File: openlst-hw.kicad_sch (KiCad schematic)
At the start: 85 parts, among them J1 Battery, J2 CC Prog/Debug, J3 UART0, J4 SPI0, J5 Control Outputs, J6 ANT, U1 LP2981-3.3, U2 CC1110, U3 AP6502, U4 ASFL1-27.000MHZ, U5 MIC803, U6 PE4250, U8 SF2446E, U9 RFFM6404

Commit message: changed connectors, halfway through pcb
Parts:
- removed C12: 0.1u, Capacitor_SMD:C_0603_1608Metric, symbol openlst-hw:C_Small
- removed C13: 0.01u, Capacitor_SMD:C_0603_1608Metric, symbol openlst-hw:C_Small
- removed C14: 6.8n, Capacitor_SMD:C_0603_1608Metric, symbol Device:C
- removed C15, C16: 22u, Capacitor_SMD:C_1210_3225Metric, symbol Device:C
- removed C17, C18, C4: 10u, Capacitor_SMD:C_0805_2012Metric, symbol Device:C
- removed J1: Battery, TerminalBlock_Phoenix:TerminalBlock_Phoenix_MKDS-1,5-2-5.08_1x02_P5.08mm_Horizontal, symbol Connector:Screw_Terminal_01x02
- removed J2: CC Prog/Debug, Connector_PinHeader_1.27mm:PinHeader_2x05_P1.27mm_Vertical_SMD, symbol openlst-hw:Conn_02x05_Odd_Even
- removed J3: UART0, Connector_PinHeader_2.54mm:PinHeader_1x06_P2.54mm_Vertical, symbol openlst-hw:Conn_01x06
- removed J4: SPI0, Connector_PinHeader_2.54mm:PinHeader_1x06_P2.54mm_Vertical, symbol openlst-hw:Conn_01x06
- removed J5: Control Outputs, Connector_PinHeader_2.54mm:PinHeader_1x03_P2.54mm_Vertical, symbol openlst-hw:Conn_01x03
- removed L1: 10u, Inductor_SMD:L_Vishay_IFSC-1515AH_4x4x1.8mm, symbol Device:L
- removed R10, R13, R14, R9: 100, Resistor_SMD:R_0603_1608Metric, symbol openlst-hw:R
- removed R15: 6k8, Resistor_SMD:R_0603_1608Metric, symbol Device:R
- removed R19: 36k, Resistor_SMD:R_0603_1608Metric, symbol Device:R
- removed R20: 10k, Resistor_SMD:R_0603_1608Metric, symbol Device:R
- removed U1: LP2981-3.3, Package_TO_SOT_SMD:SOT-23-5, symbol Regulator_Linear:LP2985-3.3
- removed U3: AP6502, openlst:SOIC-8-1EP_3.9x4.9mm_P1.27mm_EP2.613x3.502mm, symbol Regulator_Switching:AP6502
- removed U9: RFFM6404, openlst:Qorvo_LGA_28_ThermalVias, symbol openlst-hw:RFFM6404
- added J3: Conn_02x10_Odd_Even, satfab_3rdparty:ERM8-010-YY.Y-XXX-DV-TR, symbol Connector_Generic:Conn_02x10_Odd_Even
- added U7: RFFM6406, openlst:Qorvo_LGA_28_ThermalVias, symbol openlst-hw:RFFM6406
- J6: footprint Connector_Coaxial:SMA_Samtec_SMA-J-P-X-ST-EM1_EdgeMount -> satfab_3rdparty:SAMTEC_MMCXV-J-P-HF-ST-TH1; ManufPN SMA-J-P-H-ST-EM1 -> MMCXV-J-P-HF-ST-TH1; SupplierPN SMA-J-P-H-ST-EM1 -> MMCXV-J-P-HF-ST-TH1
- L2, L3, L8: Manuf Pulse Electronics Network -> Wurth; ManufPN PE-0603FB102ST -> 74279266; SupplierPN 553-2381-1-ND -> 732-4484-1-ND
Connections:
- net +3V3: now also J3.4 (Pin_4)
- net GND: now also J3.1 (Pin_1), J3.17 (Pin_17), J3.19 (Pin_19), J3.2 (Pin_2), J3.20 (Pin_20), U7.1 (GND), U7.11 (GND), U7.12 (GND), U7.15 (GND), U7.19 (GND), U7.21 (GND), U7.22 (GND), U7.27 (GND), U7.28 (GND), U7.29 (PAD), U7.6 (GND), U7.8 (GND), U7.9 (GND)
- net LST_TX_MODE: now also U7.2 (TR)
- net PROG_DC: now also J3.16 (Pin_16)
- net PROG_DD: now also J3.18 (Pin_18)
- net RF_BYP: now also U7.4 (BYP)
- net RF_EN: now also U7.3 (EN)
- net VAA: now also J3.3 (Pin_3), J3.5 (Pin_5)
- net VAA_FILT: now also U7.17 (VCC_RX), U7.23 (VDD), U7.24 (VCC_TX1), U7.26 (VCC_TX2)
- net ~{LST_RESET}: now also J3.14 (Pin_14)
- net at C45.2: now also U7.7 (ANT)
- net at C6.1, R36.1, R37.2: now also U7.5 (VAPC)
- net at C38.2: now also U7.18 (RX)
- net at C39.2: now also U7.20 (TX)
- net at U8.2 (IN): now also U7.10 (SAW1)
- net at U8.5 (OUT): now also U7.13 (SAW2)
- net CAN_CS renamed UART1_CTS
- net CAN_MISO renamed UART1_RX
- net CAN_MOSI renamed UART1_TX
- net CAN_SCK renamed UART1_RTS
- new net UART_CTS_0: J3.12 (Pin_12)
- new net UART_RTS_0: J3.6 (Pin_6)
- new net UART_RX_0: J3.10 (Pin_10)
- new net UART_TX_0: J3.8 (Pin_8)
- no-connect marks 10 -> 9
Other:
- note removed: "4.255 V"
- note removed: "SPI Headers (3.3 V)"
- note removed: "UART Headers (3.3 V)"
- moved on the sheet: C45, H1, H2, H3, H4

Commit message: finished edits v1
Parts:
- added TP1, TP2: TestPoint, satfab:RCUCTE_0603_Test_Point, symbol Connector:TestPoint
- D1, D2, R3, R4: now not fitted
- H1, H2, H3, H4: now left out of the parts list
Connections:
- net UART_CTS_0 is gone; now on net ~{LST_RESET}: J3.12 (Pin_12)
- net UART_RTS_0 is gone; now on net UART_TX_1: J3.6 (Pin_6)
- net UART_RX_0 is gone; now on net UART_CTS_1: J3.10 (Pin_10)
- net UART_TX_0 is gone; now on net UART_RTS_1: J3.8 (Pin_8)
- net PROG_DC: now also J3.18 (Pin_18); no longer J3.16 (Pin_16)
- net PROG_DD: now also J3.16 (Pin_16); no longer J3.18 (Pin_18)
- net UART0_RX: now also TP1.1
- net UART0_TX: now also TP2.1
- net ~{LST_RESET}: no longer J3.14 (Pin_14)
- net AN1: no longer names the net of U2.6 (P0_1)
- net UART1_CTS renamed UART_CTS_1
- net UART1_RTS renamed UART_RTS_1
- net UART1_RX renamed UART_RX_1
- net UART_RX_1: now also J3.14 (Pin_14)
- net UART1_TX renamed UART_TX_1
- no-connect marks 9 -> 16

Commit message: finished edits v2
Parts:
- H1, H2, H3, H4: footprint MountingHole:MountingHole_3.2mm_M3 -> MountingHole:MountingHole_3.2mm_M3_Pad_Via; symbol Mechanical:MountingHole -> Mechanical:MountingHole_Pad; now in the parts list
- L2: footprint Inductor_SMD:L_0603_1608Metric -> Inductor_SMD:L_1206_3216Metric; Manuf Wurth -> Laird; ManufPN 74279266 -> MI1206L501R-10; SupplierPN 732-4484-1-ND -> 240-2407-2-ND
- TP1, TP2: Manuf (none) -> KOA; ManufPN (none) -> RCUCTE; Supplier (none) -> Digikey; SupplierPN (none) -> 2019-RCUCTETR-ND
- U7: Manuf (none) -> Qorvo; ManufPN (none) -> RFFM6406SR; Supplier (none) -> Mouser; SupplierPN (none) -> 772-RFFM6406SR
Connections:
- net GND: now also H1.1, H2.1, H3.1, H4.1
- net PROG_DC: now also J3.6 (Pin_6); no longer J3.18 (Pin_18)
- net PROG_DD: now also J3.8 (Pin_8); no longer J3.16 (Pin_16)
- net UART_CTS_1: now also J3.14 (Pin_14); no longer J3.10 (Pin_10)
- net UART_RTS_1: now also J3.16 (Pin_16); no longer J3.8 (Pin_8)
- net UART_RX_1: now also J3.10 (Pin_10); no longer J3.14 (Pin_14)
- net UART_TX_1: now also J3.18 (Pin_18); no longer J3.6 (Pin_6)
- no-connect marks 16 -> 15
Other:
- moved on the sheet: C1, C10, C11, C19, C2, C21, C22, C23, C24, C25, C26, C27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

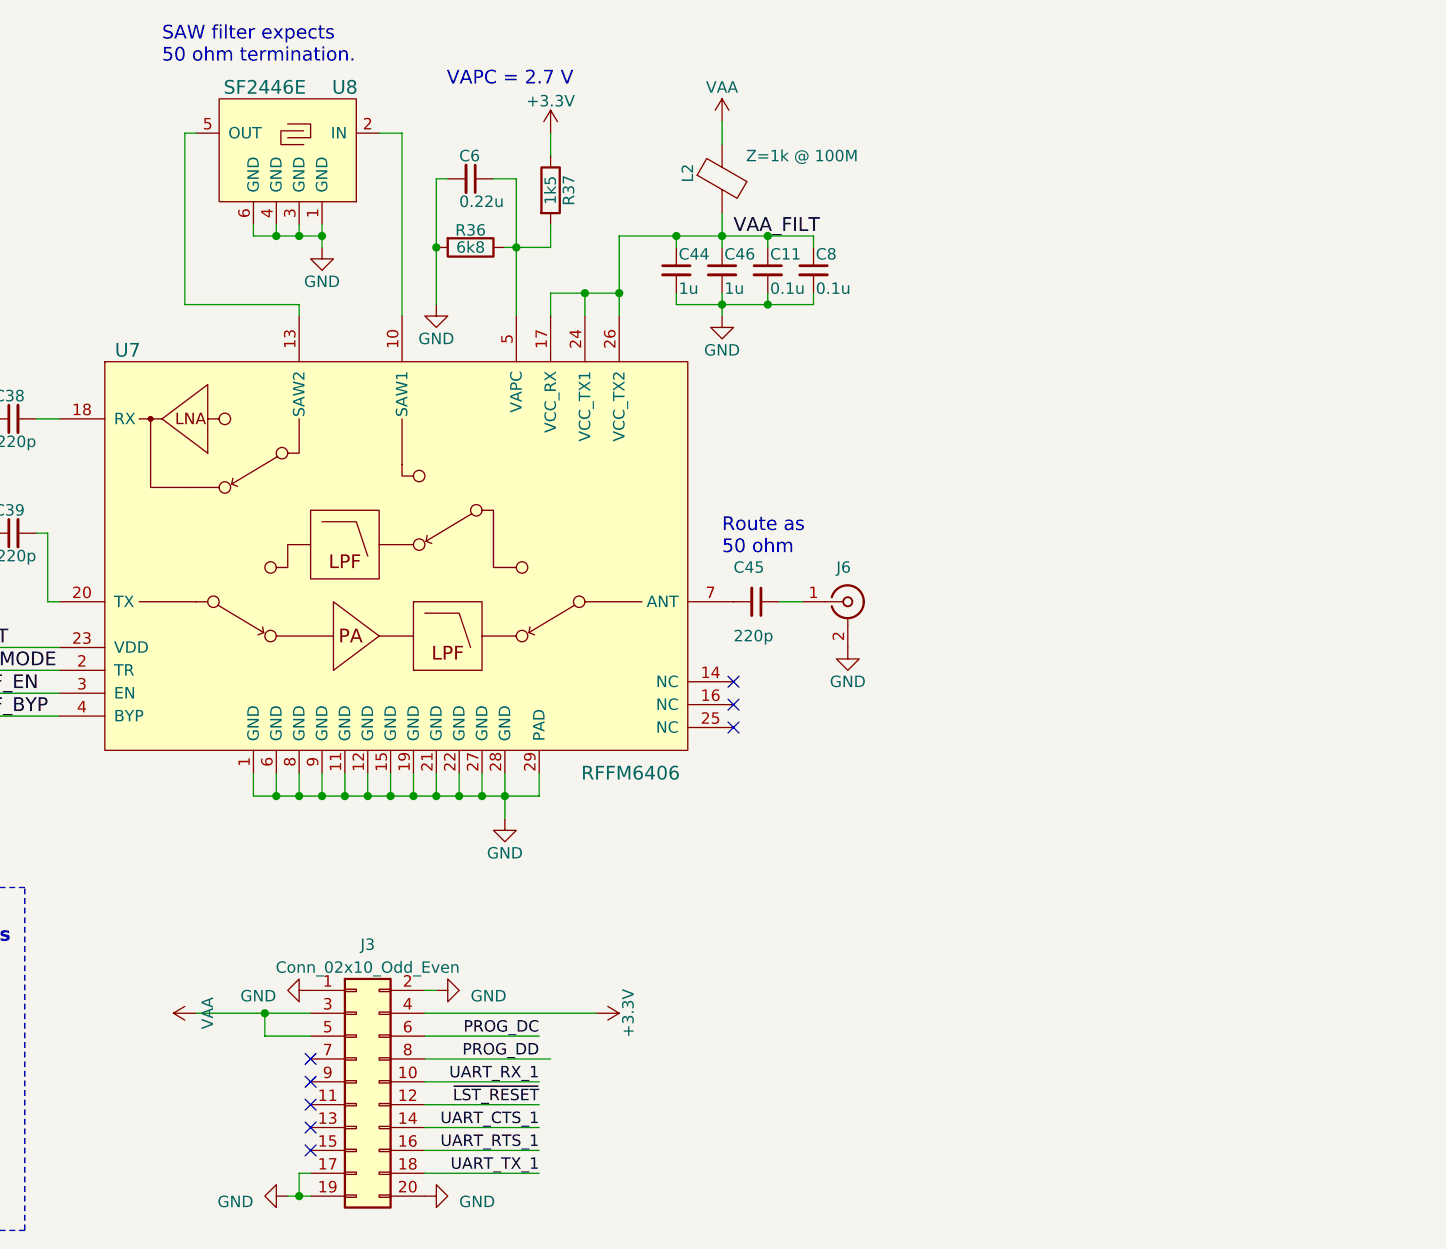
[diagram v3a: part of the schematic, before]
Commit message: added thermal reliefs and thermistors
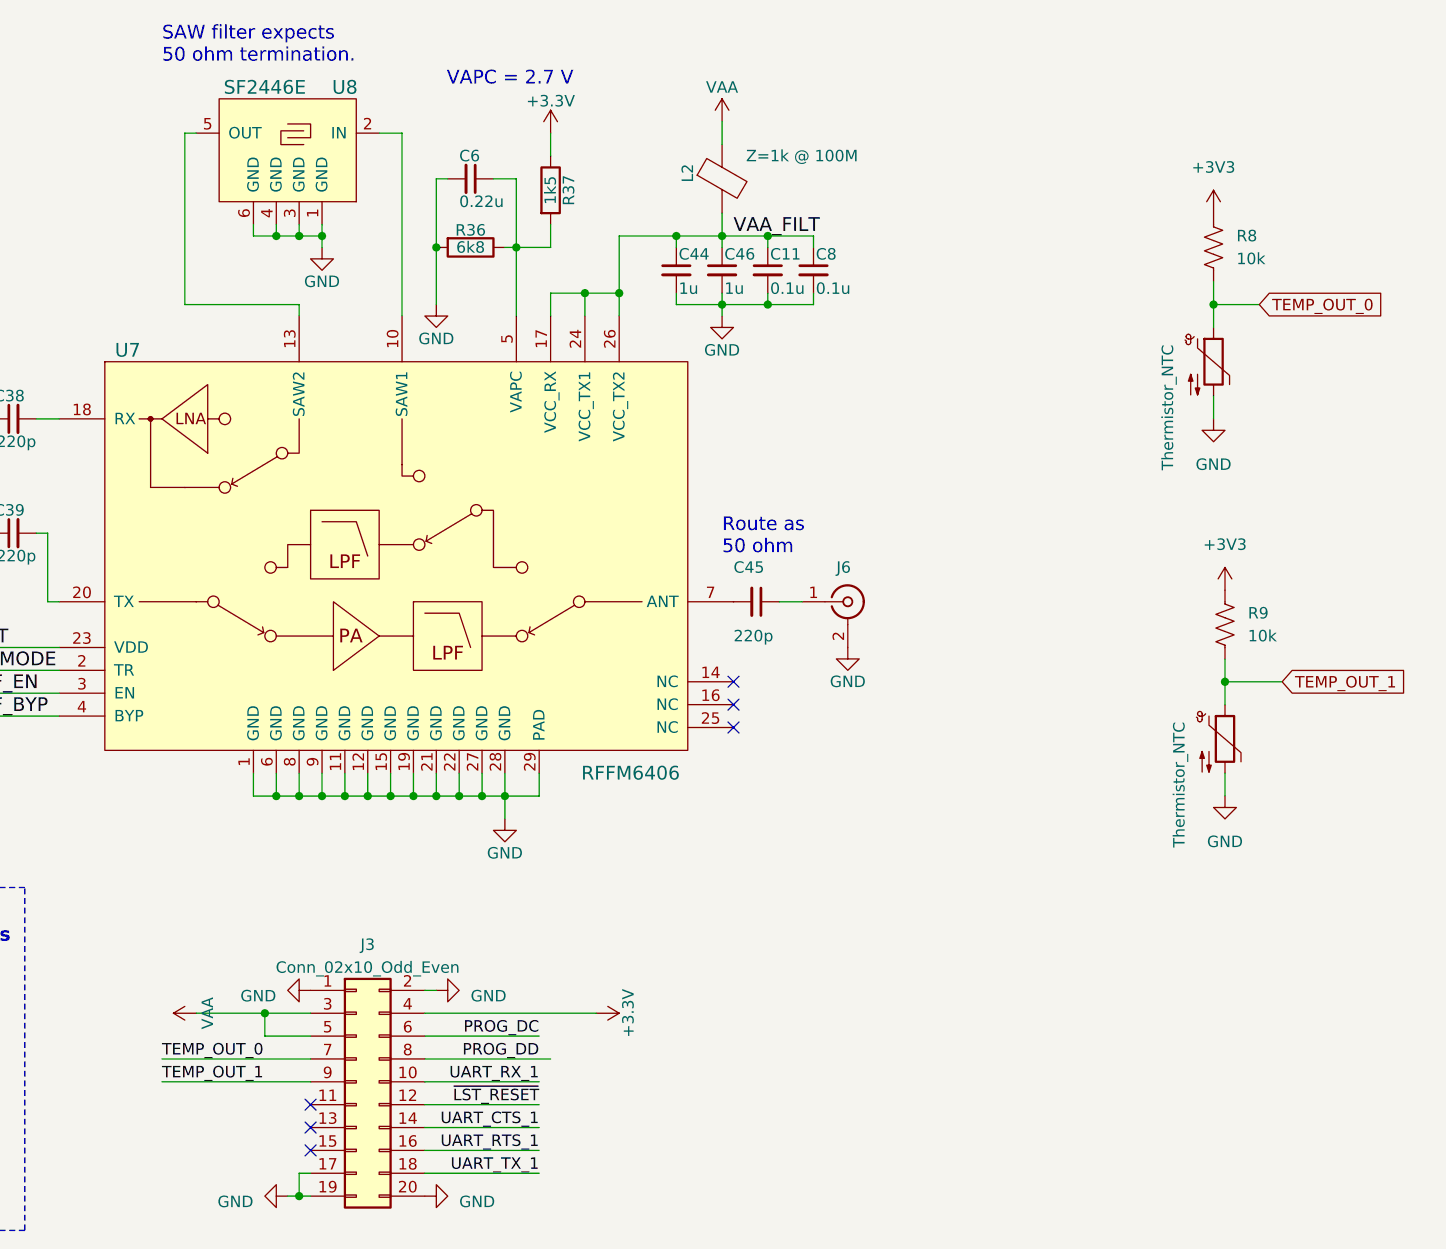
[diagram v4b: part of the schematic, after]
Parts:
- added R8, R9: 10k, Resistor_SMD:R_0603_1608Metric, symbol Device:R_US
- added TH1, TH2: Thermistor_NTC, Resistor_SMD:R_0805_2012Metric, symbol Device:Thermistor_NTC
- J3: ManufPN ERM8-005-02.0-L-DV-TR -> ERM8-010-02.0-L-DV-TR; SupplierPN SAM13674TR-ND -> SAM13683CT-ND
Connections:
- net +3V3: now also R8.1, R9.1
- net GND: now also TH1.2, TH2.2
- net TEMP_OUT_0: now reaches J3.7 (Pin_7)
- net TEMP_OUT_0: now also R8.2, TH1.1
- net TEMP_OUT_1: now reaches J3.9 (Pin_9)
- net TEMP_OUT_1: now also R9.2, TH2.1
- no-connect marks 15 -> 13

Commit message: changed thermistor part numbers
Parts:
- TH1, TH2: Digikey PN A106104CT-ND -> 273-TX08F103F3435ERCT-ND; MPN NTC0805J10K -> TX08F103F3435ER; Manuf (none) -> Ohmite; ManufPN (none) -> TX08F103F3435ER; Supplier (none) -> Digikey; SupplierPN (none) -> 273-TX08F103F3435ERCT-ND
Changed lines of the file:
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@@
       (effects (font (size 1.27 1.27)) hide)
     )
-    (property "MPN" "NTC0805J10K" (at 342.9 102.87 90)
+    (property "MPN" "TX08F103F3435ER" (at 342.9 102.87 90)
       (effects (font (size 1.27 1.27)) hide)
     )
-    (property "Digikey PN" "A106104CT-ND" (at 342.9 102.87 90)
+    (property "Digikey PN" "273-TX08F103F3435ERCT-ND" (at 342.9 102.87 90)
+      (effects (font (size 1.27 1.27)) hide)
+    )
+    (property "Manuf" "Ohmite" (at 342.9 102.87 0)
+      (effects (font (size 1.27 1.27)) hide)
+    )
+    (property "ManufPN" "TX08F103F3435ER" (at 342.9 102.87 0)
+      (effects (font (size 1.27 1.27)) hide)
+    )
+    (property "Supplier" "Digikey" (at 342.9 102.87 0)
+      (effects (font (size 1.27 1.27)) hide)
+    )
+    (property "SupplierPN" "273-TX08F103F3435ERCT-ND" (at 342.9 102.87 0)
       (effects (font (size 1.27 1.27)) hide)
     )
@@
       (effects (font (size 1.27 1.27)) hide)
     )
-    (property "MPN" "NTC0805J10K" (at 344.17 144.78 90)
+    (property "MPN" "TX08F103F3435ER" (at 344.17 144.78 90)
       (effects (font (size 1.27 1.27)) hide)
     )
-    (property "Digikey PN" "A106104CT-ND" (at 344.17 144.78 90)
+    (property "Digikey PN" "273-TX08F103F3435ERCT-ND" (at 344.17 144.78 90)
       (effects (font (size 1.27 1.27)) hide)
     )
+    (property "Manuf" "Ohmite" (at 344.17 144.78 0)
+      (effects (font (size 1.27 1.27)) hide)
+    )
+    (property "ManufPN" "TX08F103F3435ER" (at 344.17 144.78 0)
+      (effects (font (size 1.27 1.27)) hide)
+    )
+    (property "Supplier" "Digikey" (at 344.17 144.78 0)
+      (effects (font (size 1.27 1.27)) hide)
+    )
+    (property "SupplierPN" "273-TX08F103F3435ERCT-ND" (at 344.17 144.78 0)
+      (effects (font (size 1.27 1.27)) hide)
+    )

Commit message: changed bom to reflect obc
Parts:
- C1, C10, C11, C26, C3, C5, C8: ManufPN CL10B104MB8NNNC -> CL10B104KB8NNWC; SupplierPN 1276-1941-1-ND -> 1276-1935-1-ND
- C19, C22: ManufPN 06035C102KAT2A -> 0603B102K500CT; SupplierPN 478-1215-1-ND -> 1292-1380-1-ND
- C44, C46, C47, C9: ManufPN CL10B105MO8NNWC -> CL10A105KA8NNNC; SupplierPN 1276-6524-1-ND -> 1276-1102-1-ND
- R1, R18, R2, R26, R28, R3, R4: Manuf Yageo -> Stackpole Electronics; ManufPN RC0603FR-071KL -> RMCF0603FT1K00; SupplierPN 311-1.00KHRCT-ND -> RMCF0603FT1K00CT-ND
- R22: Manuf Yageo -> (none); ManufPN RC0603FR-0710KL -> WR06X103 JTL; SupplierPN 311-10.0KHRCT-ND -> 1292-WR06X103JTLCT-ND
- R8, R9: Digikey PN 1292-WR06X103JTLCT-ND -> (none); MPN WR06X103 JTL -> (none); ManufPN (none) -> WR06X103 JTL; Supplier (none) -> Digikey; SupplierPN (none) -> 1292-WR06X103JTLCT-ND
- TH1, TH2: Digikey PN 273-TX08F103F3435ERCT-ND -> (none); MPN TX08F103F3435ER -> (none)

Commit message: adjusted BOM headers
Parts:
- C1, C10, C11, C26, C3, C5, C8: MPN (none) -> CL10B104KB8NNWC; ManufPN CL10B104KB8NNWC -> (none)
- C19, C22: MPN (none) -> 0603B102K500CT; ManufPN 0603B102K500CT -> (none)
- C2, C21, C25, C38, C39, C45, C7: MPN (none) -> GCM1555C1H221JA16D; ManufPN GCM1555C1H221JA16D -> (none)
- C23, C24: MPN (none) -> AC0402CRNPO9BN3R9; ManufPN AC0402CRNPO9BN3R9 -> (none)
- C27: MPN (none) -> GCM188R72A103KA37D; ManufPN GCM188R72A103KA37D -> (none)
- C44, C46, C47, C9: MPN (none) -> CL10A105KA8NNNC; ManufPN CL10A105KA8NNNC -> (none)
- C6: MPN (none) -> CL10B224KO8NNNC; ManufPN CL10B224KO8NNNC -> (none)
- D1, D2: MPN (none) -> 150060VS75000; ManufPN 150060VS75000 -> (none)
- J3: MPN (none) -> ERM8-010-02.0-L-DV-TR; ManufPN ERM8-010-02.0-L-DV-TR -> (none)
- J6: MPN (none) -> MMCXV-J-P-HF-ST-TH1; ManufPN MMCXV-J-P-HF-ST-TH1 -> (none)
- L2: MPN (none) -> MI1206L501R-10; ManufPN MI1206L501R-10 -> (none)
- L3, L8: MPN (none) -> 74279266; ManufPN 74279266 -> (none)
- L5, L6: MPN (none) -> LQW15AN27NJ00D; ManufPN LQW15AN27NJ00D -> (none)
- R1, R18, R2, R26, R28, R3, R4: MPN (none) -> RMCF0603FT1K00; ManufPN RMCF0603FT1K00 -> (none)
- R11, R12, R17, R5, R6, R7, R8: MPN (none) -> RC0603FR-07100RL; ManufPN RC0603FR-07100RL -> (none)
- R16: MPN (none) -> RC0603FR-0756KL; ManufPN RC0603FR-0756KL -> (none)
- R21, R27: MPN (none) -> RMCF0603FT33K0; ManufPN RMCF0603FT33K0 -> (none)
- R22, R8, R9: MPN (none) -> WR06X103 JTL; ManufPN WR06X103 JTL -> (none)
- R36: MPN (none) -> RC0603FR-076K8L; ManufPN RC0603FR-076K8L -> (none)
- R37: MPN (none) -> ERJ-3EKF1501V; ManufPN ERJ-3EKF1501V -> (none)
- TH1, TH2: MPN (none) -> TX08F103F3435ER; ManufPN TX08F103F3435ER -> (none)
- TP1, TP2: MPN (none) -> RCUCTE; ManufPN RCUCTE -> (none)
- U2: MPN (none) -> CC1110F32; ManufPN CC1110F32RHHR -> (none); Supplier Texas Instruments -> Mouser; SupplierPN CC1110F32RHHR -> 595-CC1110F32RHHR
- U4: MPN (none) -> ASFL1-27.000MHZ-EK-T; ManufPN ASFL1-27.000MHZ-EK-T -> (none)
- U5: MPN (none) -> MIC803-29D3VM3-TR; ManufPN MIC803-29D3VM3-TR -> (none)
- U6: MPN (none) -> PE4250MLI-Z; ManufPN PE4250MLI-Z -> (none)
- U7: MPN (none) -> RFFM6406SR; ManufPN RFFM6406SR -> (none)
- U8: MPN (none) -> SF2446E; ManufPN SF2446E -> (none); SupplierPN 2410-SF2446E-ND -> 198-SF2446E

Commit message: fixed typo in bom
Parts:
- R36: Supplier Digkey -> Digikey
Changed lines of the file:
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@@
       (effects (font (size 1.27 1.27)) hide)
     )
-    (property "Supplier" "Digkey" (at 262.89 88.265 0)
+    (property "Supplier" "Digikey" (at 262.89 88.265 0)
       (effects (font (size 1.27 1.27)) hide)
     )
